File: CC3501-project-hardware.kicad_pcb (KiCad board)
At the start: 4 copper layers, 85 x 56 mm, 115 parts, among them J1 USB_C_Receptacle_USB2.0_16P, J4 Conn_01x03_Socket, J5 Conn_01x04_Socket, J6 Conn_01x08_Socket, J7 Conn_01x04, J8 Conn_01x06_Socket, J9 Conn_01x02_Socket, P2 Header 1.27mm 2x5 PTH, P3 Header 3, Q1 SS8550, Q3 AO3401A, Q4 AO3401A, SW1 SW_Push, SW2 SW_Push, SW3 SW_Push, U1 RP2040, U3 MFRC52202HN(TOKMAS), U4 SY8089A1AAC, U7 HX711, U8 W25Q128JVSIQTR, Y1 X322512MSB4SI, Y2 Crystal_GND23

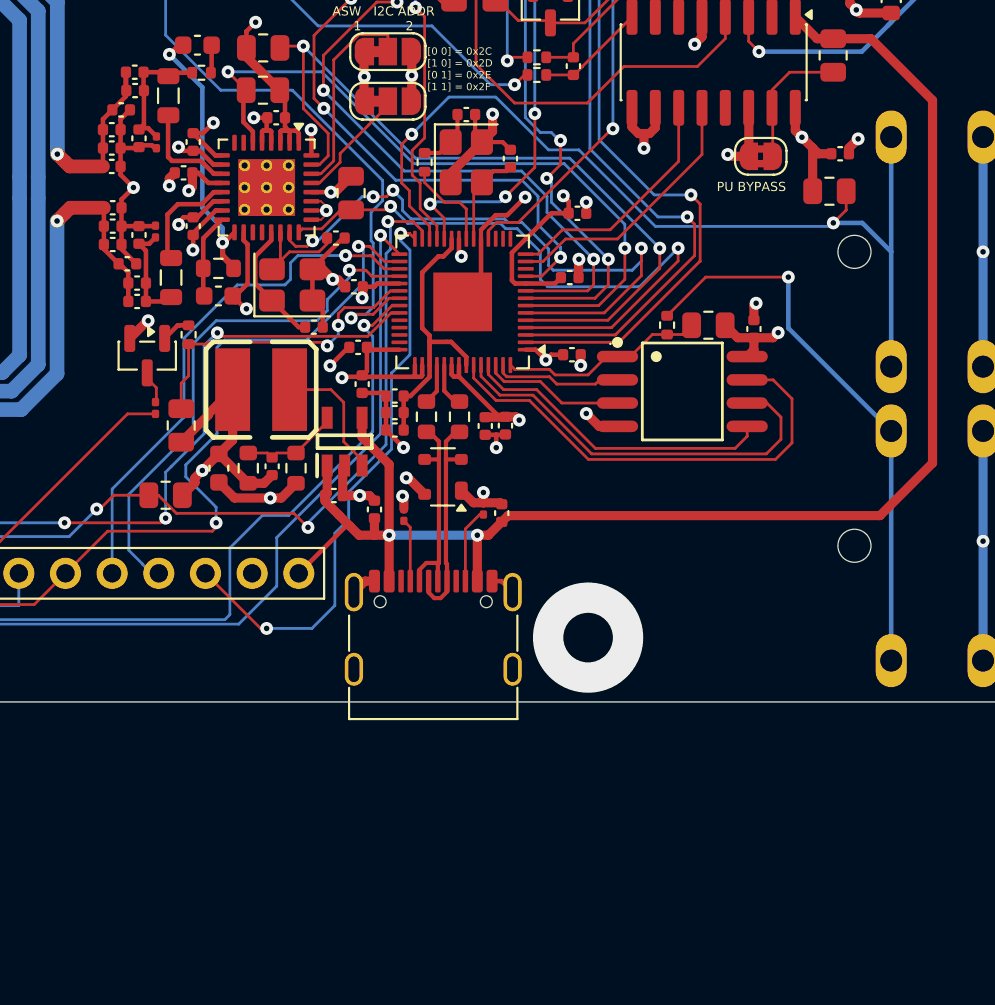
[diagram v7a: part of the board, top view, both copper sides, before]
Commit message: updated R1,R2 position on pcb
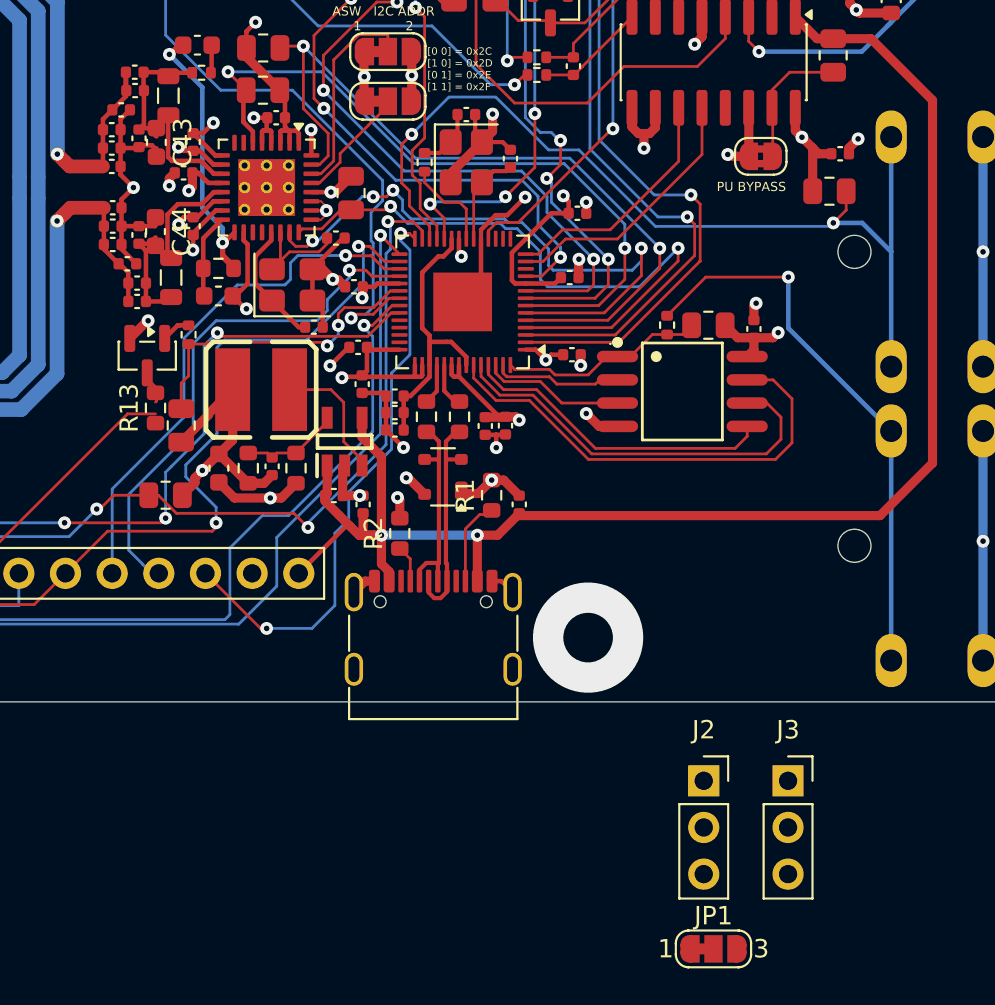
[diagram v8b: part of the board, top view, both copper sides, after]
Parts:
- added J2: Conn_01x03_Socket, Connector_PinSocket_2.54mm:PinSocket_1x03_P2.54mm_Vertical, F.Cu at (187.8, 85.3)
- added J3: Conn_01x03_Socket, Connector_PinSocket_2.54mm:PinSocket_1x03_P2.54mm_Vertical, F.Cu at (192.4, 85.3)
- added JP1: SolderJumper_3_Bridged12, Jumper:SolderJumper-3_P1.3mm_Bridged12_RoundedPad1.0x1.5mm_NumberLabels, F.Cu at (188.3, 94.4)
- C43, C44: footprint Capacitor_SMD:C_0201_0603Metric -> Capacitor_SMD:C_0603_1608Metric
- R1, R13, R2: footprint Resistor_SMD:R_0201_0603Metric -> Resistor_SMD:R_0603_1608Metric
- moved C40 1.06 mm to (177.8, 70.2)
- moved R2 1.02 mm to (171.2, 71.8)
- moved R1 0.86 mm to (176.2, 69.8)
- moved C19 0.68 mm to (169.2, 70.2)
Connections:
- C1 pad 2: Net-(U4-FB) -> Net-(IC1-FB)
- L1 pad 2: Net-(U4-LX) -> Net-(IC1-LX)
- R8 pad 2: Net-(U4-FB) -> Net-(IC1-FB)
- R9 pad 1: Net-(U4-FB) -> Net-(IC1-FB)
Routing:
- net Net-(J1-CC1): track 3.42 -> 2.01 mm
- net +5V: track 101.0 -> 101.9 mm
- net GND: track 155.0 -> 155.6 mm
- net Net-(J1-CC2): track 4.15 -> 4.69 mm
